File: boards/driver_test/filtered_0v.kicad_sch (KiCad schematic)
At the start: 3 parts

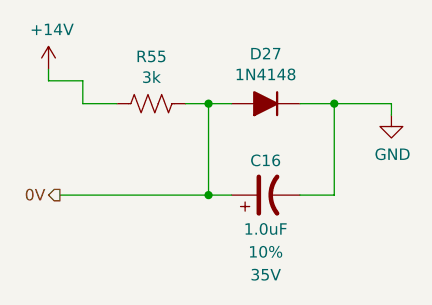
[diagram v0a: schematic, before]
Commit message: Driver test: finished up board layout
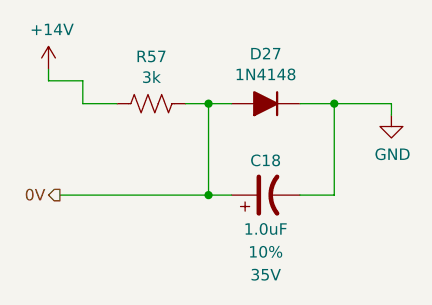
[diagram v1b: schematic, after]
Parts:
- renumbered C16 to C18, R55 to R57
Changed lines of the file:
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@@
   (symbol (lib_id "Device:C_Polarized_US") (at 129.54 101.6 90) (unit 1)
     (in_bom yes) (on_board yes)
-    (property "Reference" "C16" (id 0) (at 129.54 97.79 90))
+    (property "Reference" "C18" (id 0) (at 129.54 97.79 90))
     (property "Value" "1.0uF" (id 1) (at 129.54 105.41 90))
     (property "Footprint" "Capacitor_Tantalum_SMD:CP_EIA-3528-21_Kemet-B" (id 2) (at 129.54 101.6 0)
@@
   (symbol (lib_id "lachesis:+14V") (at 105.41 87.63 0) (unit 1)
     (in_bom yes) (on_board yes)
-    (property "Reference" "#PWR049" (id 0) (at 105.41 91.44 0)
+    (property "Reference" "#PWR053" (id 0) (at 105.41 91.44 0)
       (effects (font (size 1.27 1.27)) hide)
     )
@@
   (symbol (lib_id "Device:R_US") (at 116.84 91.44 270) (unit 1)
     (in_bom yes) (on_board yes)
-    (property "Reference" "R55" (id 0) (at 116.84 86.233 90))
+    (property "Reference" "R57" (id 0) (at 116.84 86.233 90))
     (property "Value" "3k" (id 1) (at 116.84 88.5444 90))
     (property "Footprint" "Resistor_SMD:R_0603_1608Metric" (id 2) (at 116.586 92.456 90)
@@
   (symbol (lib_id "power:GND") (at 143.51 92.71 0) (unit 1)
     (in_bom yes) (on_board yes)
-    (property "Reference" "#PWR050" (id 0) (at 143.51 99.06 0)
+    (property "Reference" "#PWR054" (id 0) (at 143.51 99.06 0)
       (effects (font (size 1.27 1.27)) hide)
     )
